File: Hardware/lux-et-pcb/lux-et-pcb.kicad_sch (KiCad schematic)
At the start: 87 parts, among them J1 Conn_01x03_Socket, J2 Conn_01x03_Socket, J3 Conn_01x03_Socket, J4 USB_C_Receptacle_PowerOnly_6P, Q1 PMOS, Q2 PMOS, Q3 AO3400A, Q4 AO3400A, Q5 AO3400A, Q7 2N7002K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

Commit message: BoM update
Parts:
- removed J4: USB_C_Receptacle_PowerOnly_6P, Library:USB-C-SMD_GT-USB-7101A, symbol Connector:USB_C_Receptacle_PowerOnly_6P
- added J5: USB_C_Receptacle_USB2.0_8P, Library:USB-C-SMD_GT-USB-7101A, symbol New_Library:USB_C_Receptacle_USB2.0_8P
- C4, CD1, CD3: LCSC C77075 -> C380331
- C7: LCSC C162422 -> C380331
- D10, D5, D6, D7, D8, D9: LCSC 1 -> C2843785
- L2: LCSC 1 -> C108962
- PORT1, PORT3: LCSC 1 -> C7433470
- PORT2: LCSC (none) -> C7433470
- PROG1, RST1: LCSC 1 -> C2888502
- Q3, Q4, Q5: LCSC (none) -> C347497
- R27, R28: LCSC C -> C27834
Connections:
- net GND: now also J5.A12 (GND), J5.B12 (GND), J5.S1 (SHIELD)
- net at R28.2: now also J5.A5 (CC1)
- net at D15.2 (A): now also J5.A9 (VBUS), J5.B9 (VBUS)
- net at R27.2: now also J5.B5 (CC2)
- new net USB_M: J5.A7 (D-)
- new net USB_P: J5.A6 (D+)
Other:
- note added: "Circle LEDs"
- note added: "PORT2"
- note removed: "Aditional IOs"
- note removed: "Status LEDs"
- moved on the sheet: Batt1, C10, C11, C4, C7, C8, CC1, CD1, CD2, CD3, CD4, CD5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

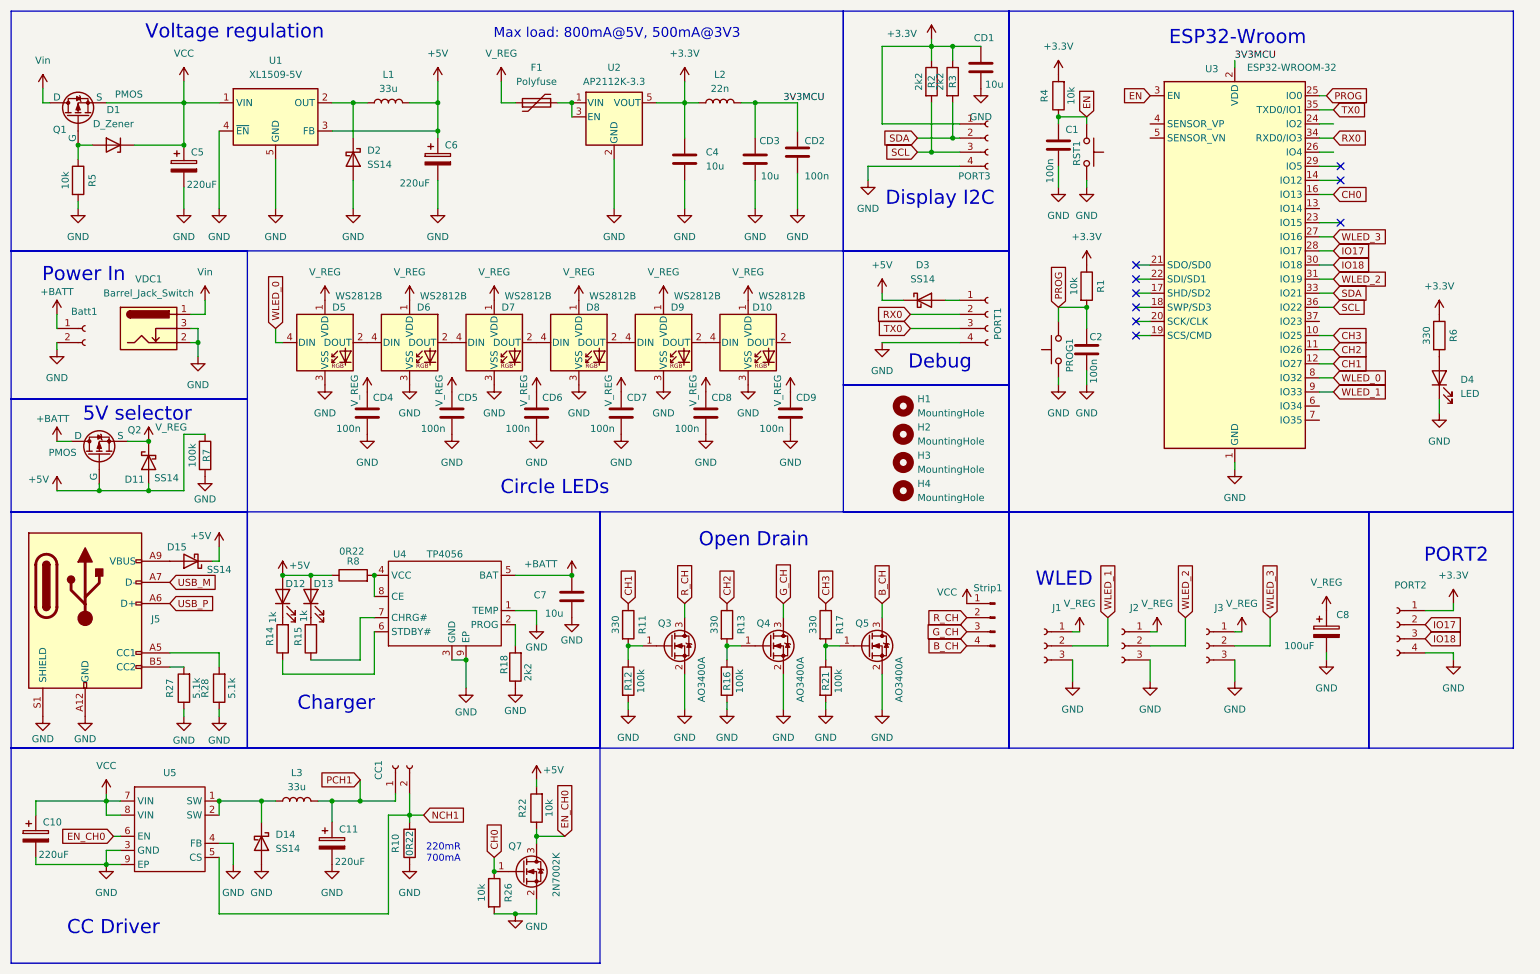
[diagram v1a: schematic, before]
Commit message: Added V2 placeholder sketch
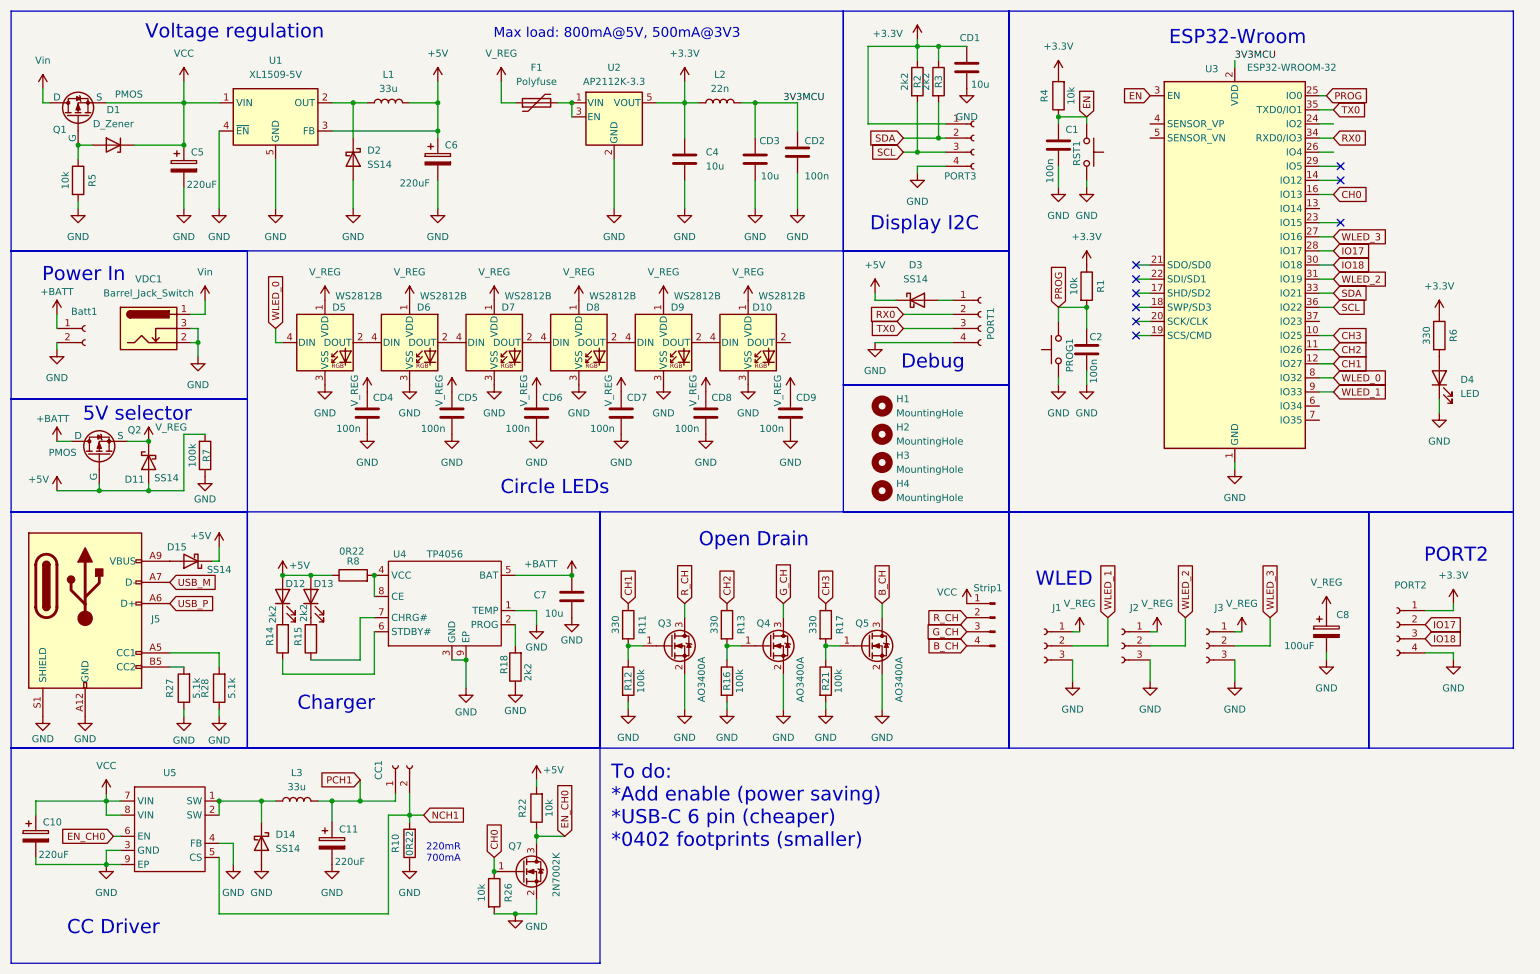
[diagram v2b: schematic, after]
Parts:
- R14, R15: value 1k -> 2k2; LCSC C11702 -> C17520
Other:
- note added: "To do: *Add enable (power saving) *USB-C 6 pin (cheaper) *0402 footprints (smaller)"
- moved on the sheet: CD1, D3, H1, H2, H3, H4, PORT1, PORT3, R2, R3

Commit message: Hardware update
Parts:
- R11, R13, R17, R6: value 330 -> 330R
- R14, R15, R18, R2, R3: value 2k2 -> 2.2k
- U5: value ~ -> XL4001
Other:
- note added: "To do: *Add enable (power saving) *USB-C 6 pin (cheaper) *0402 footprints (smaller) *Change PMOS to SOT-23"
- note removed: "To do: *Add enable (power saving) *USB-C 6 pin (cheaper) *0402 footprints (smaller)"
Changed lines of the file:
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@@
 		)
 	)
-	(text "To do:\n*Add enable (power saving)\n*USB-C 6 pin (cheaper)\n*0402 footprints (smaller)"
+	(text "To do:\n*Add enable (power saving)\n*USB-C 6 pin (cheaper)\n*0402 footprints (smaller)\n*Change PMOS to SOT-23"
 		(exclude_from_sim no)
 		(at 121.412 157.226 0)
@@
 			)
 		)
-		(property "Value" "330"
+		(property "Value" "330R"
 			(at 139.954 124.46 90)
 			(effects
@@
 			)
 		)
-		(property "Value" "2k2"
+		(property "Value" "2.2k"
 			(at 66.04 123.952 90)
 			(effects
@@
 			)
 		)
-		(property "Value" "2k2"
+		(property "Value" "2.2k"
 			(at 106.426 134.62 90)
 			(effects
@@
 			)
 		)
-		(property "Value" "2k2"
+		(property "Value" "2.2k"
 			(at 178.054 26.67 90)
 			(effects
@@
 			)
 		)
-		(property "Sim.Pins" "1=D 2=G 3=S"
+		(property "Sim.Pins" "1=G 2=D 3=S"
 			(at 40.64 33.02 0)
 			(effects
@@
 			)
 		)
-		(property "Value" "330"
+		(property "Value" "330R"
 			(at 122.174 124.46 90)
 			(effects
@@
 			)
 		)
-		(property "Value" "2k2"
+		(property "Value" "2.2k"
 			(at 60.452 124.206 90)
 			(effects
@@
 		(on_board yes)
 		(dnp no)
-		(fields_autoplaced yes)
 		(property "Reference" "U5"
-			(at 41.91 151.13 0)
+			(at 41.91 150.368 0)
 			(effects
 				(font
@@
 			)
 		)
-		(property "Value" "~"
-			(at 41.91 153.67 0)
+		(property "Value" "XL4001"
+			(at 41.91 152.654 0)
 			(effects
 				(font
@@
 			)
 		)
-		(property "Value" "330"
+		(property "Value" "330R"
 			(at 157.734 124.46 90)
 			(effects
@@
 			)
 		)
-		(property "Value" "2k2"
+		(property "Value" "2.2k"
 			(at 174.244 26.67 90)
 			(effects
@@
 			)
 		)
-		(property "Value" "330"
+		(property "Value" "330R"
 			(at 268.224 72.39 90)
 			(effects

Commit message: Case update
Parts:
- C8: value 100uF -> 220uF
- D4: value LED -> LED_GREEN
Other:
- note added: "To do: *Add enable (power saving) *0402 footprints (smaller) *Change PMOS to SOT-23 *Correct PMOS pinout"
- note removed: "To do: *Add enable (power saving) *USB-C 6 pin (cheaper) *0402 footprints (smaller) *Change PMOS to SOT-23"
